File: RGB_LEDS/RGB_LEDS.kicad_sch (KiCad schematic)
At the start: 16 parts, among them IC1 ATTINY202-SSFR, IC2 INA180A4IDBVR, IC3 XC9140A501MR-G, J1 HCZZ0021-2, SW1 SW_Push, U1 MY-2032-08

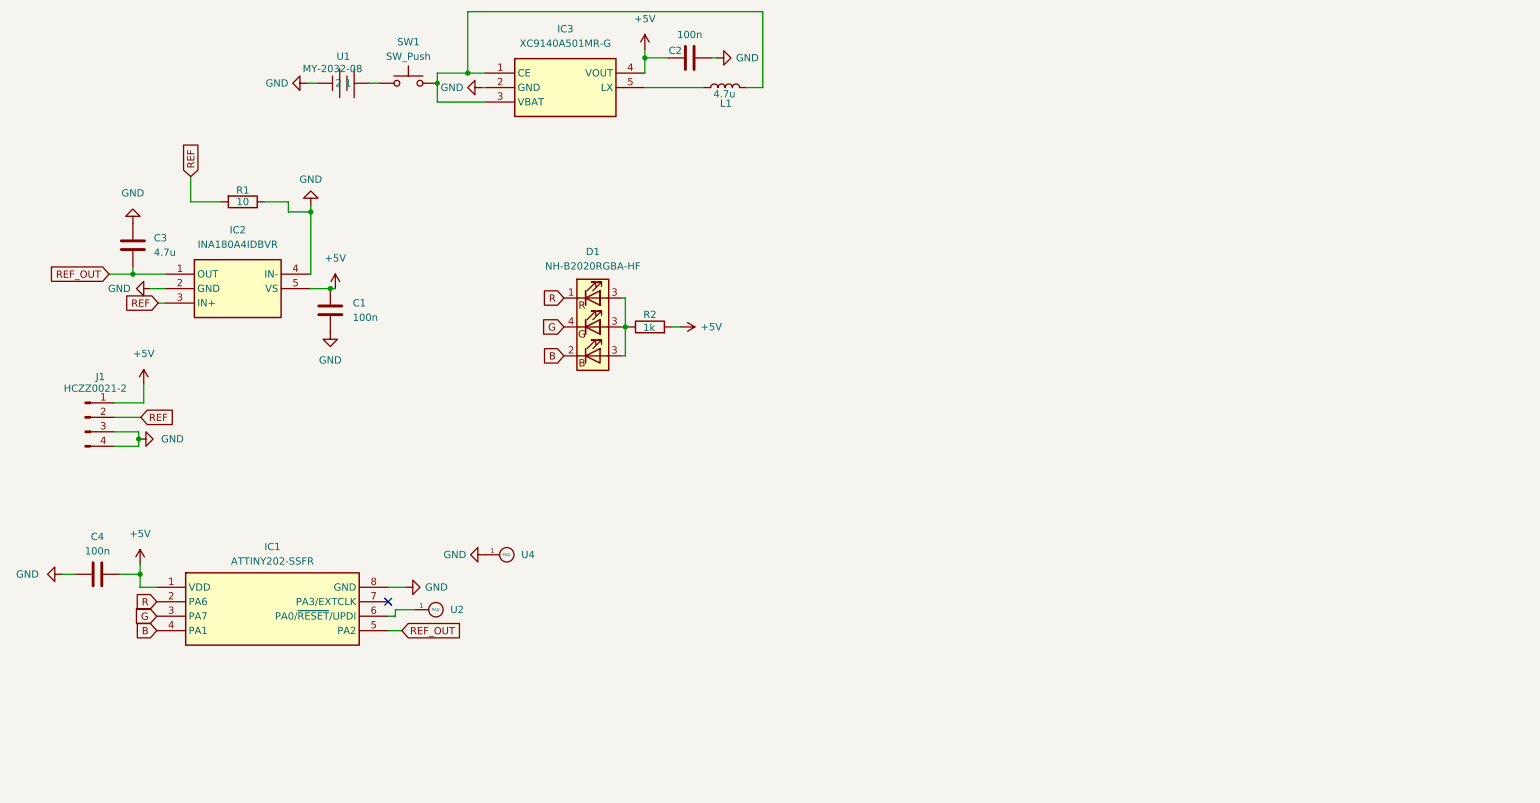
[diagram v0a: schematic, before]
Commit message: Placa con stm32, selector de voltaje se necesita quitar una vez que se decida por un valor
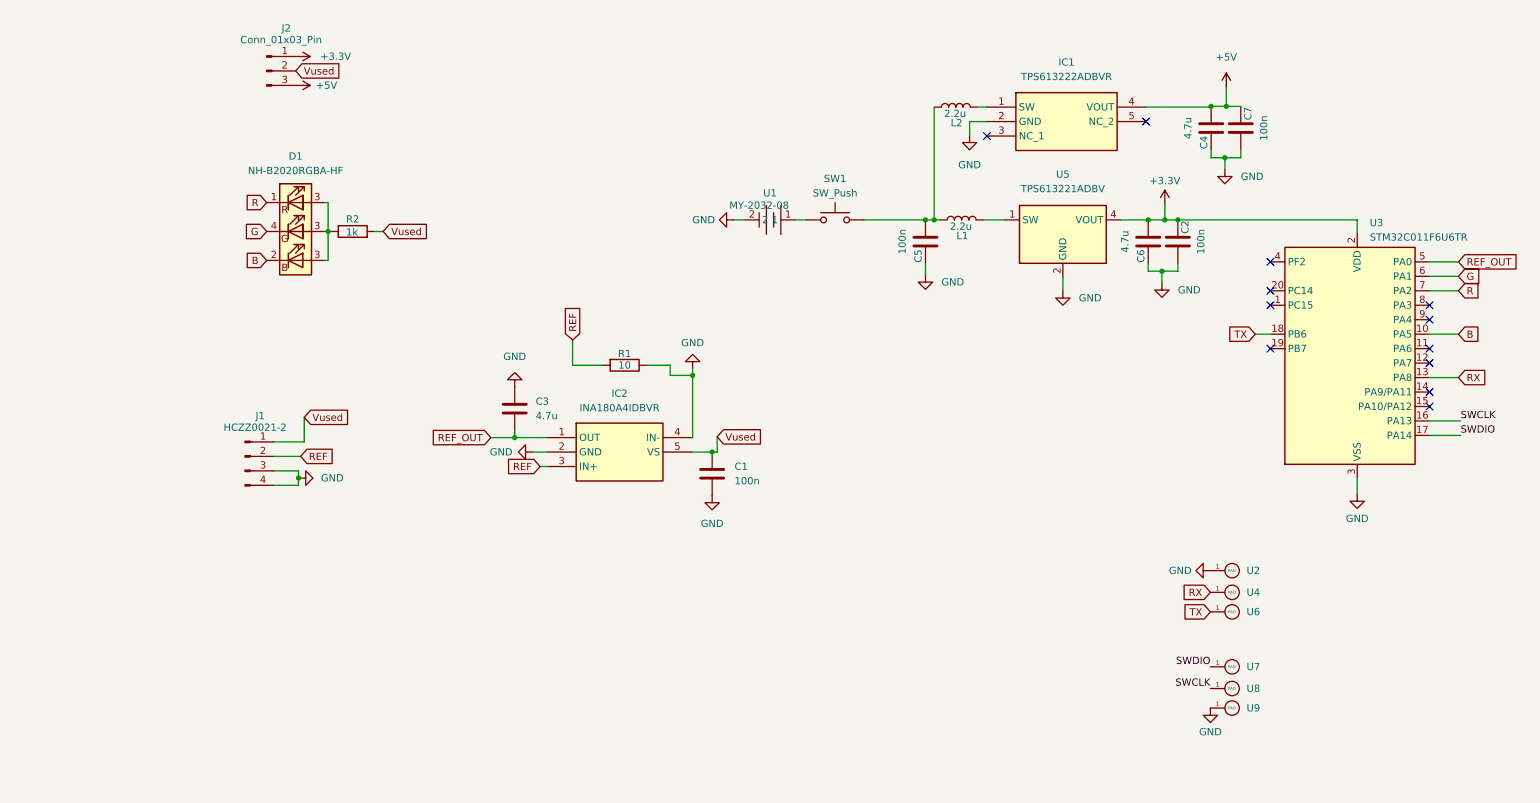
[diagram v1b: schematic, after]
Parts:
- removed IC1: ATTINY202-SSFR, SamacSys_Parts:SOIC127P600X175-8N, symbol SamacSys_Parts:ATTINY202-SSFR
- removed IC3: XC9140A501MR-G, SamacSys_Parts:SOT95P280X130-5N, symbol SamacSys_Parts:XC9140A501MR-G
- added C5, C7: 100n, Capacitor_SMD:C_0402_1005Metric, symbol Device:C
- added C6: 4.7u, Capacitor_SMD:C_0402_1005Metric, symbol Device:C
- added IC1: TPS613222ADBVR, SamacSys_Parts:SOT95P280X145-5N, symbol SamacSys_Parts:TPS613222ADBVR
- added J2: Conn_01x03_Pin, Connector_PinHeader_2.54mm:PinHeader_1x03_P2.54mm_Vertical, symbol Connector:Conn_01x03_Pin
- added L2: 2.2u, Inductor_SMD:L_0805_2012Metric, symbol Device:L
- added U3: STM32C011F6U6TR, Package_DFN_QFN:ST_UFQFPN-20_3x3mm_P0.5mm, symbol MCU_ST_STM32C0:STM32C011F4Ux
- added U5: TPS613221ADBV, Package_TO_SOT_SMD:SOT-23-5, symbol Regulator_Switching:TPS613221ADBV
- added U6, U7, U8, U9: ~, TestPoint:TestPoint_Pad_1.0x1.0mm, symbol Pads:PAD
- C2: footprint Capacitor_SMD:C_0603_1608Metric -> Capacitor_SMD:C_0402_1005Metric
- C4: value 100n -> 4.7u; footprint Capacitor_SMD:C_0603_1608Metric -> Capacitor_SMD:C_0402_1005Metric
- L1: value 4.7u -> 2.2u
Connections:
- net +5V: now also C7.2, IC1.4 (VOUT), J2.3 (Pin_3); no longer C1.1, C2.2, IC2.5 (VS), J1.1 (Pin_1), R2.2
- net B: now also U3.10 (PA5)
- net G: now also U3.6 (PA1)
- net GND: now also U1.2, U2.1 (PAD), C5.2, C6.2, C7.1, IC1.2 (GND), U3.3 (VSS), U5.2 (GND), U9.1 (PAD); no longer U1. (2), U4.1 (PAD)
- net R: now also U3.7 (PA2)
- net REF_OUT: now also U3.5 (PA0)
- net at SW1.1: now also U1.1; no longer U1. (2)
- net at SW1.2: now also L1.1, C5.1, L2.1; no longer L1.2
- new net: L1.2, U5.1 (SW)
- new net: IC1.1 (SW), L2.2
- new net +3.3V: C2.2, C6.1, J2.1 (Pin_1), U3.2 (VDD), U5.4 (VOUT)
- new net RX: U3.13 (PA8), U4.1 (PAD)
- new net SWCLK: U3.16 (PA13), U8.1 (PAD)
- new net SWDIO: U3.17 (PA14), U7.1 (PAD)
- new net TX: U3.18 (PB6), U6.1 (PAD)
- new net Vused: C1.1, IC2.5 (VS), J1.1 (Pin_1), J2.2 (Pin_2), R2.2
- no-connect marks 1 -> 12
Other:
- moved on the sheet: C1, C3, D1, IC2, L1, R1, R2, SW1

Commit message: final version, longer connector, 3.3 only
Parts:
- removed C4: 4.7u, Capacitor_SMD:C_0402_1005Metric, symbol Device:C
- removed C7: 100n, Capacitor_SMD:C_0402_1005Metric, symbol Device:C
- removed IC1: TPS613222ADBVR, SamacSys_Parts:SOT95P280X145-5N, symbol SamacSys_Parts:TPS613222ADBVR
- removed J1: HCZZ0021-2, Library:CONN-SMD_2P-P2.50-A2501-WF-02A, symbol Connector:Conn_01x04_Pin
- removed J2: Conn_01x03_Pin, Connector_PinHeader_2.54mm:PinHeader_1x03_P2.54mm_Vertical, symbol Connector:Conn_01x03_Pin
- removed L2: 2.2u, Inductor_SMD:L_0805_2012Metric, symbol Device:L
- added J2: 22122021, CONN_A-4094-02A_MOL, symbol 0022122021:22122021
- IC2: footprint SamacSys_Parts:SOT95P280X145-5N -> SamacSys:SOT95P280X145-5N
- SW1: value SW_Push -> TSC015A05026A
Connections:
- net Vused is gone; now on net +3.3V: C1.1, IC2.5 (VS), R2.2
- net +3.3V: now also J2.2
- net REF: now also J2.1
- no-connect marks 12 -> 10

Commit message: Added selector
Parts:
- added S1: CL-SB-23B-01T, CLSB23B01T, symbol SamacSys_Parts:CL-SB-23B-01T
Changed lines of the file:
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@@
+    )
+  )
+  (symbol (lib_id "SamacSys_Parts:CL-SB-23B-01T") (at 88.138 145.415 0) (unit 1)
+    (in_bom yes) (on_board yes) (dnp no) (fields_autoplaced)
+    (property "Reference" "S1" (at 103.378 138.43 0)
+      (effects (font (size 1.27 1.27)))
+    )
+    (property "Value" "CL-SB-23B-01T" (at 103.378 140.97 0)
+      (effects (font (size 1.27 1.27)))
+    )
+    (property "Footprint" "CLSB23B01T" (at 114.808 240.335 0)
+      (effects (font (size 1.27 1.27)) (justify left top) hide)
+    )
+    (property "Datasheet" "http://www.farnell.com/datasheets/2604289.pdf" (at 114.808 340.335 0)
+      (effects (font (size 1.27 1.27)) (justify left top) hide)
+    )
+    (property "Height" "3.5" (at 114.808 540.335 0)
+      (effects (font (size 1.27 1.27)) (justify left top) hide)
+    )
+    (property "Manufacturer_Name" "Nidec Copal" (at 114.808 640.335 0)
+      (effects (font (size 1.27 1.27)) (justify left top) hide)
+    )
+    (property "Manufacturer_Part_Number" "CL-SB-23B-01T" (at 114.808 740.335 0)
+      (effects (font (size 1.27 1.27)) (justify left top) hide)
+    )
+    (property "Mouser Part Number" "229-CL-SB-23B-01T" (at 114.808 840.335 0)
+      (effects (font (size 1.27 1.27)) (justify left top) hide)
+    )
+    (property "Mouser Price/Stock" "https://www.mouser.co.uk/ProductDetail/Nidec-Components/CL-SB-23B-01T?qs=XeJtXLiO41QX0zcc2Dzzgg%3D%3D" (at 114.808 940.335 0)
+      (effects (font (size 1.27 1.27)) (justify left top) hide)
+    )
+    (property "Arrow Part Number" "" (at 114.808 1040.335 0)
+      (effects (font (size 1.27 1.27)) (justify left top) hide)
+    )
+    (property "Arrow Price/Stock" "" (at 114.808 1140.335 0)
+      (effects (font (size 1.27 1.27)) (justify left top) hide)
+    )
+    (pin "5")
+    (pin "7")
+    (pin "8")
+    (pin "2")
+    (pin "3")
+    (pin "1")
+    (pin "4")
+    (pin "6")
+    (instances
+      (project "RGB_LEDS"
+        (path "/a07b2659-588e-42c7-8d6e-3a495304319d"
+          (reference "S1") (unit 1)
+        )
+      )
     )
   )
